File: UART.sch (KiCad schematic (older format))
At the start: 6 parts, among them Y1 Crystal

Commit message: UART
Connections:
- net labels added: Address, Data, INTR, IO-M', RD', Reset, WR'
- wire segments 39 -> 107
- no-connect marks 3 -> 12
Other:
- moved on the sheet: J?, U?

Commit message: Merged 8254
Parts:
- gave numbers to parts that had none: 5
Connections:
- net IO-M' renamed M-IO'
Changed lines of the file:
@@
 $Descr A4 11693 8268
 encoding utf-8
-Sheet 6 6
+Sheet 5 8
 Title ""
 Date ""
@@
 $EndDescr
 $Comp
-L DSUB-9:DSUB-9 J?
+L DSUB-9:DSUB-9 J2
 U 1 1 6249A35C
 P 9500 2150
-F 0 "J?" V 9839 2278 60  0000 L CNN
+F 0 "J2" V 9839 2278 60  0000 L CNN
 F 1 "DSUB-9" V 9945 2278 60  0000 L CNN
 F 2 "DSUB-9" H 10100 1790 60  0001 C CNN
@@
 $EndComp
 $Comp
-L power:GND #PWR?
+L power:GND #PWR0149
 U 1 1 6249AAEF
 P 4200 3800
-F 0 "#PWR?" H 4200 3550 50  0001 C CNN
+F 0 "#PWR0149" H 4200 3550 50  0001 C CNN
 F 1 "GND" V 4205 3672 50  0000 R CNN
 F 2 "" H 4200 3800 50  0001 C CNN
@@
 $EndComp
 $Comp
-L power:GND #PWR?
+L power:GND #PWR0150
 U 1 1 6249B12C
 P 4200 3900
-F 0 "#PWR?" H 4200 3650 50  0001 C CNN
+F 0 "#PWR0150" H 4200 3650 50  0001 C CNN
 F 1 "GND" V 4205 3772 50  0000 R CNN
 F 2 "" H 4200 3900 50  0001 C CNN
@@
 $EndComp
 $Comp
-L power:GND #PWR?
+L power:GND #PWR0151
 U 1 1 6249B47B
 P 5200 4600
-F 0 "#PWR?" H 5200 4350 50  0001 C CNN
+F 0 "#PWR0151" H 5200 4350 50  0001 C CNN
 F 1 "GND" H 5205 4427 50  0000 C CNN
 F 2 "" H 5200 4600 50  0001 C CNN
@@
 $EndComp
 $Comp
-L power:GND #PWR?
+L power:GND #PWR0152
 U 1 1 6249C757
 P 4200 4100
-F 0 "#PWR?" H 4200 3850 50  0001 C CNN
+F 0 "#PWR0152" H 4200 3850 50  0001 C CNN
 F 1 "GND" V 4205 3972 50  0000 R CNN
 F 2 "" H 4200 4100 50  0001 C CNN
@@
 	4200 2400 4000 2400
 $Comp
-L Interface_UART:16550 U?
+L Interface_UART:16550 U10
 U 1 1 62498893
 P 5200 2900
-F 0 "U?" H 5200 4781 50  0000 C CNN
+F 0 "U10" H 5200 4781 50  0000 C CNN
 F 1 "16550" H 5200 4690 50  0000 C CNN
 F 2 "Package_DIP:DIP-40_W15.24mm" H 5200 2900 50  0001 C CIN
@@
 	4200 2700 4200 2800
 $Comp
-L Device:R R?
+L Device:R R11
 U 1 1 624A138D
 P 4050 2800
-F 0 "R?" V 4050 2800 50  0000 C CNN
+F 0 "R11" V 4050 2800 50  0000 C CNN
 F 1 "R" V 3934 2800 50  0000 C CNN
 F 2 "" V 3980 2800 50  0001 C CNN
@@
 Connection ~ 4200 2800
 $Comp
-L Logic_Programmable:PAL16L8 U?
+L Logic_Programmable:PAL16L8 U9
 U 1 1 624A209D
 P 3000 2700
-F 0 "U?" H 3000 3581 50  0000 C CNN
+F 0 "U9" H 3000 3581 50  0000 C CNN
 F 1 "PAL16L8" H 3000 3490 50  0000 C CNN
 F 2 "" H 3000 2700 50  0001 C CNN
@@
 	1750 4300 1750 1900
 $Comp
-L power:GND #PWR?
+L power:GND #PWR0153
 U 1 1 624C8D96
 P 9500 2550
-F 0 "#PWR?" H 9500 2300 50  0001 C CNN
+F 0 "#PWR0153" H 9500 2300 50  0001 C CNN
 F 1 "GND" H 9505 2377 50  0000 C CNN
 F 2 "" H 9500 2550 50  0001 C CNN
@@
 	6200 4100 6200 4300
 $Comp
-L max235cpg:max235cpg U?
+L max235cpg:max235cpg U11
 U 1 1 62499068
 P 8550 1400
-F 0 "U?" H 9850 1787 60  0000 C CNN
+F 0 "U11" H 9850 1787 60  0000 C CNN
 F 1 "max235cpg" H 9850 1681 60  0000 C CNN
 F 2 "max235cpg" H 9850 1640 60  0001 C CNN
@@
 NoConn ~ 8350 4000
 $Comp
-L power:GND #PWR?
+L power:GND #PWR0154
 U 1 1 6255AC9F
 P 3000 3300
-F 0 "#PWR?" H 3000 3050 50  0001 C CNN
+F 0 "#PWR0154" H 3000 3050 50  0001 C CNN
 F 1 "GND" H 3005 3127 50  0000 C CNN
 F 2 "" H 3000 3300 50  0001 C CNN
@@
 Connection ~ 8250 4000
 $Comp
-L power:GND #PWR?
+L power:GND #PWR0155
 U 1 1 6255481D
 P 8250 4000
-F 0 "#PWR?" H 8250 3750 50  0001 C CNN
+F 0 "#PWR0155" H 8250 3750 50  0001 C CNN
 F 1 "GND" H 8255 3827 50  0000 C CNN
 F 2 "" H 8250 4000 50  0001 C CNN
@@
 $EndComp
 $Comp
-L power:GND #PWR?
+L power:GND #PWR0156
 U 1 1 6255AF9D
 P 7550 1400
-F 0 "#PWR?" H 7550 1150 50  0001 C CNN
+F 0 "#PWR0156" H 7550 1150 50  0001 C CNN
 F 1 "GND" H 7550 1150 50  0000 C CNN
 F 2 "" H 7550 1400 50  0001 C CNN
@@
 RD'
 Text HLabel 1650 1500 0    50   Input ~ 0
-IO-M'
+M-IO'
 Text HLabel 1650 1800 0    50   Input ~ 0
 INTR
@@
 Reset
 $Comp
-L power:+5V #PWR?
+L power:+5V #PWR0157
 U 1 1 62583790
 P 3000 2000
-F 0 "#PWR?" H 3000 1850 50  0001 C CNN
+F 0 "#PWR0157" H 3000 1850 50  0001 C CNN
 F 1 "+5V" V 3015 2128 50  0000 L CNN
 F 2 "" H 3000 2000 50  0001 C CNN
@@
 $EndComp
 $Comp
-L power:+5V #PWR?
+L power:+5V #PWR0158
 U 1 1 62586C4F
 P 5200 1200
-F 0 "#PWR?" H 5200 1050 50  0001 C CNN
+F 0 "#PWR0158" H 5200 1050 50  0001 C CNN
 F 1 "+5V" V 5215 1328 50  0000 L CNN
 F 2 "" H 5200 1200 50  0001 C CNN
@@
 $EndComp
 $Comp
-L power:+5V #PWR?
+L power:+5V #PWR0159
 U 1 1 6258D423
 P 7450 1400
-F 0 "#PWR?" H 7450 1250 50  0001 C CNN
+F 0 "#PWR0159" H 7450 1250 50  0001 C CNN
 F 1 "+5V" H 7465 1573 50  0000 C CNN
 F 2 "" H 7450 1400 50  0001 C CNN

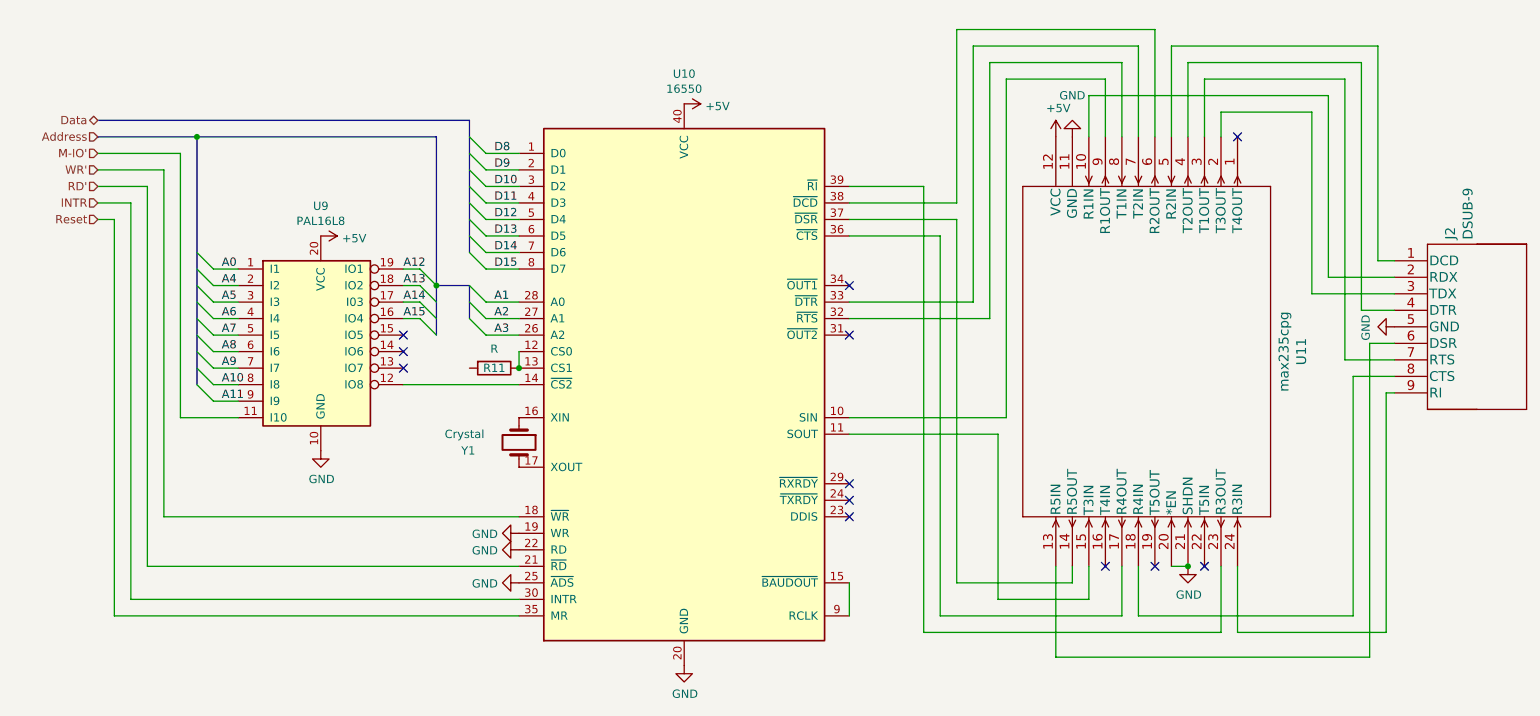
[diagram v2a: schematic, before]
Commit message: Integrated LCD.  Fixed issues with busses
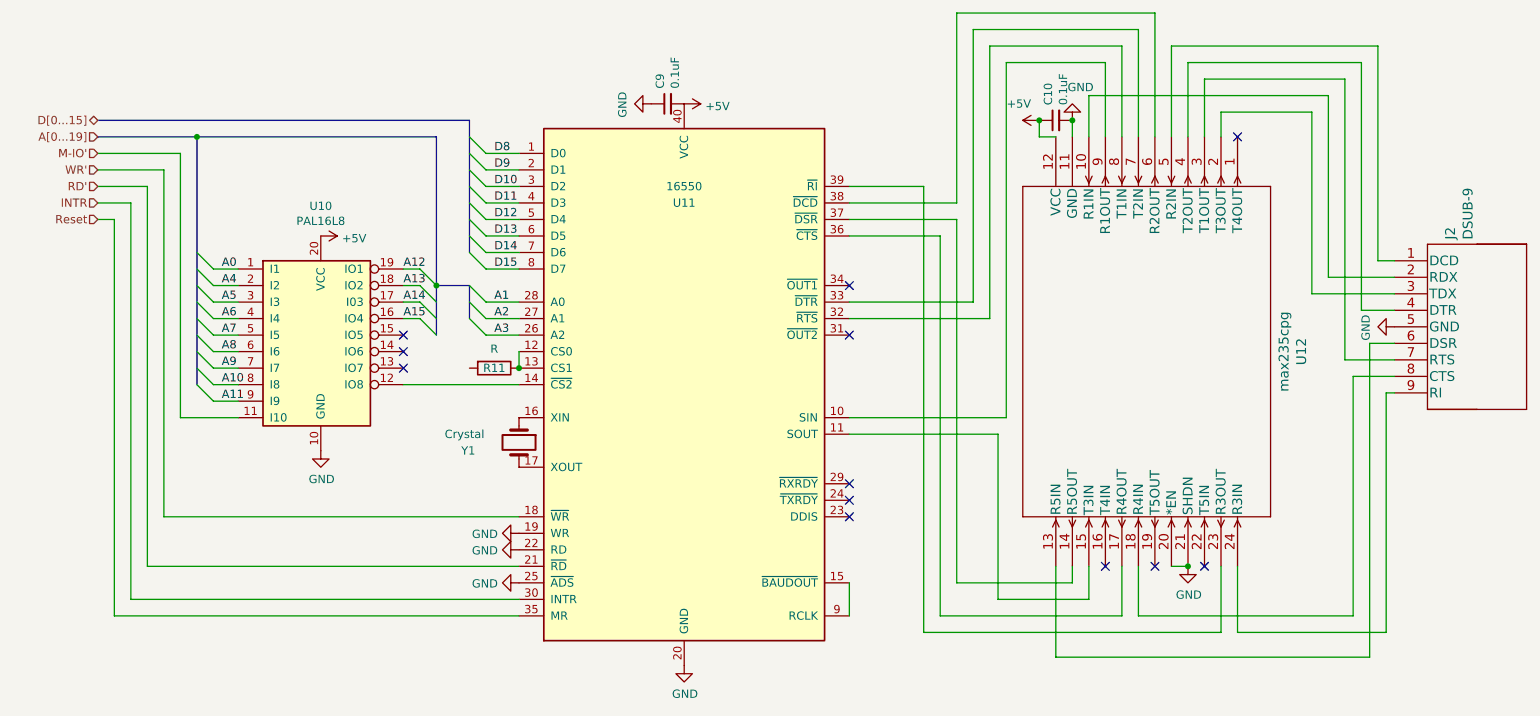
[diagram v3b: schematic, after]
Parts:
- added C10, C9: 0.1uF, symbol Device:C_Small
- renumbered U9 to U10, U10 to U11, U11 to U12
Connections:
- net +5V: now also C10.1, C9.2
- net GND: now also C10.2, C9.1
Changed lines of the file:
@@
 $Descr A4 11693 8268
 encoding utf-8
-Sheet 5 8
+Sheet 5 9
 Title ""
 Date ""
@@
 $EndComp
 $Comp
-L power:GND #PWR0149
+L power:GND #PWR059
 U 1 1 6249AAEF
 P 4200 3800
-F 0 "#PWR0149" H 4200 3550 50  0001 C CNN
+F 0 "#PWR059" H 4200 3550 50  0001 C CNN
 F 1 "GND" V 4205 3672 50  0000 R CNN
 F 2 "" H 4200 3800 50  0001 C CNN
@@
 $EndComp
 $Comp
-L power:GND #PWR0150
+L power:GND #PWR060
 U 1 1 6249B12C
 P 4200 3900
-F 0 "#PWR0150" H 4200 3650 50  0001 C CNN
+F 0 "#PWR060" H 4200 3650 50  0001 C CNN
 F 1 "GND" V 4205 3772 50  0000 R CNN
 F 2 "" H 4200 3900 50  0001 C CNN
@@
 $EndComp
 $Comp
-L power:GND #PWR0151
+L power:GND #PWR064
 U 1 1 6249B47B
 P 5200 4600
-F 0 "#PWR0151" H 5200 4350 50  0001 C CNN
+F 0 "#PWR064" H 5200 4350 50  0001 C CNN
 F 1 "GND" H 5205 4427 50  0000 C CNN
 F 2 "" H 5200 4600 50  0001 C CNN
@@
 $EndComp
 $Comp
-L power:GND #PWR0152
+L power:GND #PWR061
 U 1 1 6249C757
 P 4200 4100
-F 0 "#PWR0152" H 4200 3850 50  0001 C CNN
+F 0 "#PWR061" H 4200 3850 50  0001 C CNN
 F 1 "GND" V 4205 3972 50  0000 R CNN
 F 2 "" H 4200 4100 50  0001 C CNN
@@
 	4200 2400 4000 2400
 $Comp
-L Interface_UART:16550 U10
+L Interface_UART:16550 U11
 U 1 1 62498893
 P 5200 2900
-F 0 "U10" H 5200 4781 50  0000 C CNN
-F 1 "16550" H 5200 4690 50  0000 C CNN
+F 0 "U11" H 5200 4000 50  0000 C CNN
+F 1 "16550" H 5200 4100 50  0000 C CNN
 F 2 "Package_DIP:DIP-40_W15.24mm" H 5200 2900 50  0001 C CIN
 F 3 "http://www.ti.com/lit/ds/symlink/pc16550d.pdf" H 5200 2900 50  0001 C CNN
@@
 Connection ~ 4200 2800
 $Comp
-L Logic_Programmable:PAL16L8 U9
+L Logic_Programmable:PAL16L8 U10
 U 1 1 624A209D
 P 3000 2700
-F 0 "U9" H 3000 3581 50  0000 C CNN
+F 0 "U10" H 3000 3581 50  0000 C CNN
 F 1 "PAL16L8" H 3000 3490 50  0000 C CNN
 F 2 "" H 3000 2700 50  0001 C CNN
@@
 	1750 4300 1750 1900
 $Comp
-L power:GND #PWR0153
+L power:GND #PWR068
 U 1 1 624C8D96
 P 9500 2550
-F 0 "#PWR0153" H 9500 2300 50  0001 C CNN
+F 0 "#PWR068" H 9500 2300 50  0001 C CNN
 F 1 "GND" H 9505 2377 50  0000 C CNN
 F 2 "" H 9500 2550 50  0001 C CNN
@@
 	6200 4100 6200 4300
 $Comp
-L max235cpg:max235cpg U11
+L max235cpg:max235cpg U12
 U 1 1 62499068
 P 8550 1400
-F 0 "U11" H 9850 1787 60  0000 C CNN
+F 0 "U12" H 9850 1787 60  0000 C CNN
 F 1 "max235cpg" H 9850 1681 60  0000 C CNN
 F 2 "max235cpg" H 9850 1640 60  0001 C CNN
@@
 	6200 3100 7150 3100
 Wire Wire Line
-	7150 3100 7150 1050
-Wire Wire Line
-	7150 1050 7750 1050
-Wire Wire Line
-	7750 1050 7750 1400
+	7150 3100 7150 950
+Wire Wire Line
+	7150 950  7750 950
+Wire Wire Line
+	7750 950  7750 1400
 Wire Wire Line
 	6200 3200 7100 3200
@@
 	6200 2500 7050 2500
 Wire Wire Line
-	7050 2500 7050 950
-Wire Wire Line
-	7050 950  7850 950
-Wire Wire Line
-	7850 950  7850 1400
+	7050 2500 7050 850
+Wire Wire Line
+	7050 850  7850 850
+Wire Wire Line
+	7850 850  7850 1400
 Wire Wire Line
 	6200 1800 6850 1800
 Wire Wire Line
-	6850 1800 6850 750
-Wire Wire Line
-	6850 750  8050 750
-Wire Wire Line
-	8050 750  8050 1400
+	6850 1800 6850 650
+Wire Wire Line
+	6850 650  8050 650
+Wire Wire Line
+	8050 650  8050 1400
 Wire Wire Line
 	6200 2400 6950 2400
 Wire Wire Line
-	6950 2400 6950 850
-Wire Wire Line
-	6950 850  7950 850
-Wire Wire Line
-	7950 850  7950 1400
+	6950 2400 6950 750
+Wire Wire Line
+	6950 750  7950 750
+Wire Wire Line
+	7950 750  7950 1400
 Wire Wire Line
 	6200 1900 6850 1900
@@
 NoConn ~ 8350 4000
 $Comp
-L power:GND #PWR0154
+L power:GND #PWR058
 U 1 1 6255AC9F
 P 3000 3300
-F 0 "#PWR0154" H 3000 3050 50  0001 C CNN
+F 0 "#PWR058" H 3000 3050 50  0001 C CNN
 F 1 "GND" H 3005 3127 50  0000 C CNN
 F 2 "" H 3000 3300 50  0001 C CNN
@@
 Connection ~ 8250 4000
 $Comp
-L power:GND #PWR0155
+L power:GND #PWR067
 U 1 1 6255481D
 P 8250 4000
-F 0 "#PWR0155" H 8250 3750 50  0001 C CNN
+F 0 "#PWR067" H 8250 3750 50  0001 C CNN
 F 1 "GND" H 8255 3827 50  0000 C CNN
 F 2 "" H 8250 4000 50  0001 C CNN
@@
 	1    0    0    -1
 $EndComp
-$Comp
-L power:GND #PWR0156
-U 1 1 6255AF9D
-P 7550 1400
-F 0 "#PWR0156" H 7550 1150 50  0001 C CNN
-F 1 "GND" H 7550 1150 50  0000 C CNN
-F 2 "" H 7550 1400 50  0001 C CNN
-F 3 "" H 7550 1400 50  0001 C CNN
-	1    7550 1400
-	-1   0    0    1
-$EndComp
 Wire Wire Line
 	1750 1900 1650 1900
@@
 	1650 1300 3900 1300
 Text HLabel 1650 1300 0    50   BiDi ~ 0
-Data
+D[0...15]
 Text HLabel 1650 1400 0    50   Input ~ 0
-Address
+A[0...19]
 Text HLabel 1650 1600 0    50   Input ~ 0
 WR'
@@
 Reset
 $Comp
-L power:+5V #PWR0157
+L power:+5V #PWR057
 U 1 1 62583790
 P 3000 2000
-F 0 "#PWR0157" H 3000 1850 50  0001 C CNN
+F 0 "#PWR057" H 3000 1850 50  0001 C CNN
 F 1 "+5V" V 3015 2128 50  0000 L CNN
 F 2 "" H 3000 2000 50  0001 C CNN
@@
 $EndComp
 $Comp
-L power:+5V #PWR0158
+L power:+5V #PWR063
 U 1 1 62586C4F
 P 5200 1200
-F 0 "#PWR0158" H 5200 1050 50  0001 C CNN
+F 0 "#PWR063" H 5200 1050 50  0001 C CNN
 F 1 "+5V" V 5215 1328 50  0000 L CNN
 F 2 "" H 5200 1200 50  0001 C CNN
@@
 $EndComp
 $Comp
-L power:+5V #PWR0159
-U 1 1 6258D423
-P 7450 1400
-F 0 "#PWR0159" H 7450 1250 50  0001 C CNN
-F 1 "+5V" H 7465 1573 50  0000 C CNN
-F 2 "" H 7450 1400 50  0001 C CNN
-F 3 "" H 7450 1400 50  0001 C CNN
-	1    7450 1400
-	1    0    0    -1
+L power:GND #PWR?
+U 1 1 61C0C203
+P 5000 1200
+AR Path="/62BD3577/61C0C203" Ref="#PWR?"  Part="1"
+AR Path="/6241A5BB/61C0C203" Ref="#PWR062"  Part="1"
+F 0 "#PWR062" H 5000 950 50  0001 C CNN
+F 1 "GND" H 5005 1027 50  0000 C CNN
+F 2 "" H 5000 1200 50  0001 C CNN
+F 3 "" H 5000 1200 50  0001 C CNN
+	1    5000 1200
+	0    1    1    0
+$EndComp
+$Comp
+L Device:C_Small C?
+U 1 1 61C0C209
+P 5100 1200
+AR Path="/62BD3577/61C0C209" Ref="C?"  Part="1"
+AR Path="/6241A5BB/61C0C209" Ref="C9"  Part="1"
+F 0 "C9" H 5192 1246 50  0000 L CNN
+F 1 "0.1uF" H 5192 1155 50  0000 L CNN
+F 2 "" H 5100 1200 50  0001 C CNN
+F 3 "~" H 5100 1200 50  0001 C CNN
+	1    5100 1200
+	0    -1   -1   0
+$EndComp
+$Comp
+L Device:C_Small C?
+U 1 1 61C106FC
+P 7450 1300
+AR Path="/62BD3577/61C106FC" Ref="C?"  Part="1"
+AR Path="/6241A5BB/61C106FC" Ref="C10"  Part="1"
+F 0 "C10" H 7542 1346 50  0000 L CNN
+F 1 "0.1uF" H 7542 1255 50  0000 L CNN
+F 2 "" H 7450 1300 50  0001 C CNN
+F 3 "~" H 7450 1300 50  0001 C CNN
+	1    7450 1300
+	0    -1   -1   0
+$EndComp
+Wire Wire Line
+	7550 1300 7550 1400
+Wire Wire Line
+	7350 1300 7350 1400
+Wire Wire Line
+	7350 1400 7450 1400
+Connection ~ 7550 1300
+$Comp
+L power:GND #PWR066
+U 1 1 61C1802F
+P 7550 1300
+F 0 "#PWR066" H 7550 1050 50  0001 C CNN
+F 1 "GND" H 7500 1100 50  0000 C CNN
+F 2 "" H 7550 1300 50  0001 C CNN
+F 3 "" H 7550 1300 50  0001 C CNN
+	1    7550 1300
+	-1   0    0    1
 $EndComp
 Wire Bus Line
@@
 Wire Bus Line
 	3900 1300 3900 2100
+$Comp
+L power:+5V #PWR065
+U 1 1 61C2C387
+P 7350 1300
+F 0 "#PWR065" H 7350 1150 50  0001 C CNN
+F 1 "+5V" V 7450 1350 50  0000 L CNN
+F 2 "" H 7350 1300 50  0001 C CNN
+F 3 "" H 7350 1300 50  0001 C CNN
+	1    7350 1300
+	0    -1   -1   0
+$EndComp
+Connection ~ 7350 1300
 $EndSCHEMATC

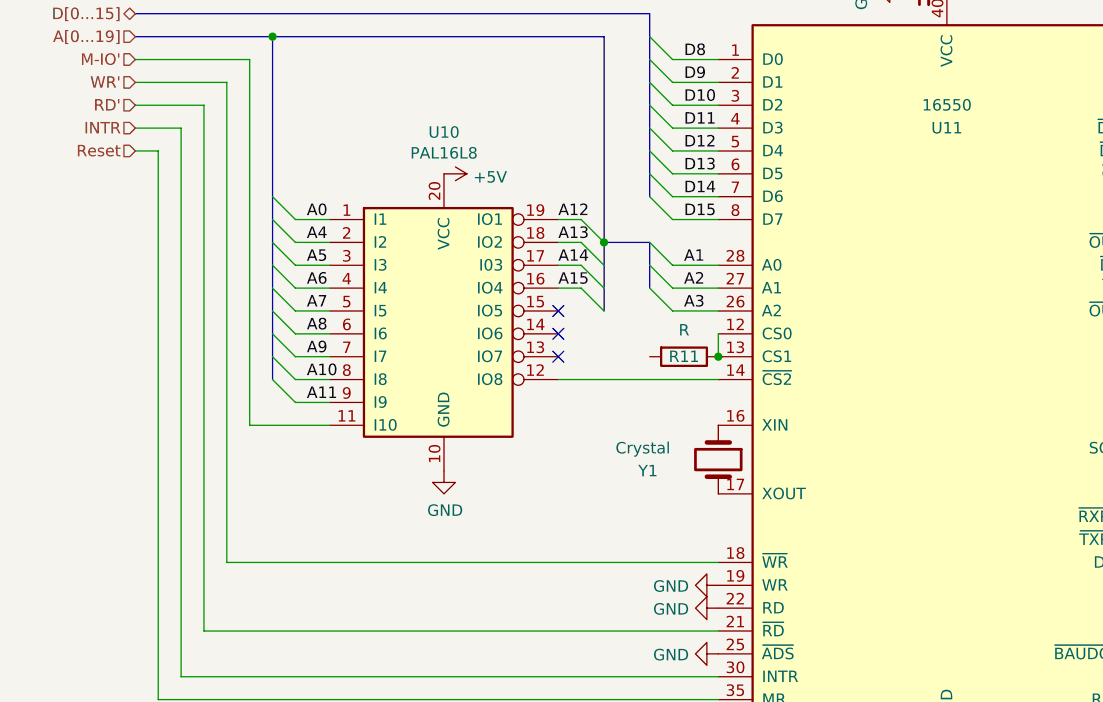
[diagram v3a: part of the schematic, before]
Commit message: All schematics present
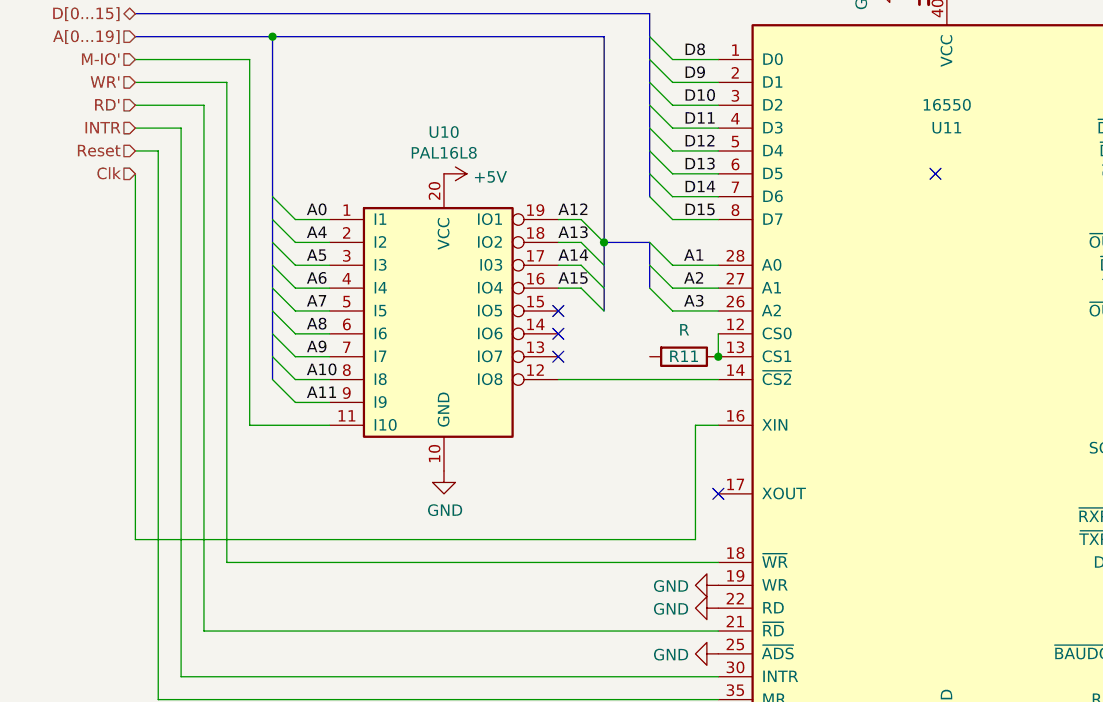
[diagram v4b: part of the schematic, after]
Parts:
- removed Y1: Crystal, symbol Device:Crystal
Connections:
- net Clk: now reaches U11.16 (XIN)
- no-connect marks 12 -> 14
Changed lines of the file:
@@
 $Descr A4 11693 8268
 encoding utf-8
-Sheet 5 9
+Sheet 5 12
 Title ""
 Date ""
@@
 	2250 1400 1650 1400
 Connection ~ 2250 1400
-$Comp
-L Device:Crystal Y1
-U 1 1 624BC21C
-P 4200 3250
-F 0 "Y1" V 4250 2900 50  0000 L CNN
-F 1 "Crystal" V 4150 2800 50  0000 L CNN
-F 2 "" H 4200 3250 50  0001 C CNN
-F 3 "~" H 4200 3250 50  0001 C CNN
-	1    4200 3250
-	0    1    1    0
-$EndComp
 Wire Wire Line
 	4200 3700 2050 3700
@@
 	-1   0    0    1
 $EndComp
-Wire Bus Line
-	3900 2300 3900 2500
-Wire Bus Line
-	3700 2300 3700 2600
-Wire Bus Line
-	2250 1400 2250 2900
-Wire Bus Line
-	3900 1300 3900 2100
 $Comp
 L power:+5V #PWR065
@@
 $EndComp
 Connection ~ 7350 1300
+NoConn ~ 5150 2000
+NoConn ~ 4200 3400
+Wire Wire Line
+	4200 3100 4100 3100
+Wire Wire Line
+	4100 3100 4100 3600
+Wire Wire Line
+	4100 3600 1650 3600
+Wire Wire Line
+	1650 3600 1650 2000
+Wire Bus Line
+	3900 2300 3900 2500
+Wire Bus Line
+	3700 2300 3700 2600
+Wire Bus Line
+	2250 1400 2250 2900
+Wire Bus Line
+	3900 1300 3900 2100
+Text HLabel 1650 2000 0    50   Input ~ 0
+Clk
 $EndSCHEMATC

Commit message: Wired Root
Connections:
- net +5V: now also R11.2
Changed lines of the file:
@@
 $Descr A4 11693 8268
 encoding utf-8
-Sheet 5 12
+Sheet 5 13
 Title ""
 Date ""
@@
 Wire Wire Line
 	1650 3600 1650 2000
-Wire Bus Line
-	3900 2300 3900 2500
-Wire Bus Line
-	3700 2300 3700 2600
-Wire Bus Line
-	2250 1400 2250 2900
-Wire Bus Line
-	3900 1300 3900 2100
 Text HLabel 1650 2000 0    50   Input ~ 0
 Clk
+Wire Bus Line
+	3900 2300 3900 2500
+Wire Bus Line
+	3700 2300 3700 2600
+Wire Bus Line
+	2250 1400 2250 2900
+Wire Bus Line
+	3900 1300 3900 2100
+$Comp
+L power:+5V #PWR?
+U 1 1 61FC357D
+P 3900 2800
+F 0 "#PWR?" H 3900 2650 50  0001 C CNN
+F 1 "+5V" V 3915 2928 50  0000 L CNN
+F 2 "" H 3900 2800 50  0001 C CNN
+F 3 "" H 3900 2800 50  0001 C CNN
+	1    3900 2800
+	0    -1   -1   0
+$EndComp
 $EndSCHEMATC
